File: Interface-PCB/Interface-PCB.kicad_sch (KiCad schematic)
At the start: 17 parts, among them J1 BARREL_JACK_PAD, J2 BARREL_JACK_PAD, J3 GPIO_DEBUG_HEADER, J4 RASPBERRYPI_GPIO_CONN_HEADER, M1 PERISTALTIC_PUMP, M2 PERISTALTIC_PUMP, M3 PERISTALTIC_PUMP, U1 TB6612FNG_BREAKOUT, U2 TB6612FNG_BREAKOUT

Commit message: Add silkscreen and logos to PCB
Complete silkscreen layer on PCB
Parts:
- added G1: PLANTER_LOGO_8mm, Interface-PCB:PLANTER_LOGO_30MM_SILKSCREEN, symbol Interface-PCB:PLANTER_LOGO_8mm
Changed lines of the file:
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@@
   (symbol (lib_id "Interface-PCB:PLANTER_LOGO_8mm") (at 247.65 29.21 0) (unit 1)
     (in_bom yes) (on_board yes) (fields_autoplaced)
-    (property "Reference" "#G1" (id 0) (at 247.65 17.3277 0)
+    (property "Reference" "G1" (id 0) (at 247.65 17.3277 0)
       (effects (font (size 1.27 1.27)) hide)
     )
@@
       (effects (font (size 1.27 1.27)) hide)
     )
-    (property "Footprint" "" (id 2) (at 247.65 29.21 0)
+    (property "Footprint" "Interface-PCB:PLANTER_LOGO_30MM_SILKSCREEN" (id 2) (at 247.65 29.21 0)
       (effects (font (size 1.27 1.27)) hide)
     )
@@
       (reference "#FLG04") (unit 1) (value "PWR_FLAG") (footprint "")
     )
-    (path "/6ae23f34-90ad-41bf-a46e-855f1c65bb29"
-      (reference "#G1") (unit 1) (value "PLANTER_LOGO_8mm") (footprint "")
-    )
     (path "/00000000-0000-0000-0000-000063fcc8a0"
       (reference "#GND01") (unit 1) (value "GND") (footprint "XXX-00000")
@@
       (reference "D3") (unit 1) (value "5V_ON") (footprint "AA_Custom_Components:LED_SS_1206_3216Metric_Pad1.42x1.75mm_HandSolder")
     )
+    (path "/6ae23f34-90ad-41bf-a46e-855f1c65bb29"
+      (reference "G1") (unit 1) (value "PLANTER_LOGO_8mm") (footprint "Interface-PCB:PLANTER_LOGO_30MM_SILKSCREEN")
+    )
     (path "/00000000-0000-0000-0000-000063bd3cac"
       (reference "H1") (unit 1) (value "MountingHole") (footprint "MountingHole:MountingHole_3.2mm_M3_Pad")
@@
       (reference "M3") (unit 1) (value "PERISTALTIC_PUMP") (footprint "AA_Custom_Components:PowerPad_Pair_5.0x5.0mm")
     )
+    (path "/00000000-0000-0000-0000-00006375997b/179f68f0-a496-4478-807a-8a228ac1fdea"
+      (reference "N1") (unit 1) (value "CENTER_POS") (footprint "AA_Custom_Components:Polarity_Center_Positive_7.5mm_SilkScreen")
+    )
+    (path "/00000000-0000-0000-0000-00006375997b/2c5f3129-e0cd-43fe-afad-b677bf741a53"
+      (reference "N2") (unit 1) (value "CENTER_POS") (footprint "AA_Custom_Components:Polarity_Center_Positive_7.5mm_SilkScreen")
+    )
+    (path "/00000000-0000-0000-0000-00006375997b/7412de6c-86c2-4352-a654-eb3ac80aac75"
+      (reference "N3") (unit 1) (value "KiCad") (footprint "Symbol:KiCad-Logo2_8mm_SilkScreen")
+    )
     (path "/00000000-0000-0000-0000-00006375997b/00000000-0000-0000-0000-000063bd2f18"

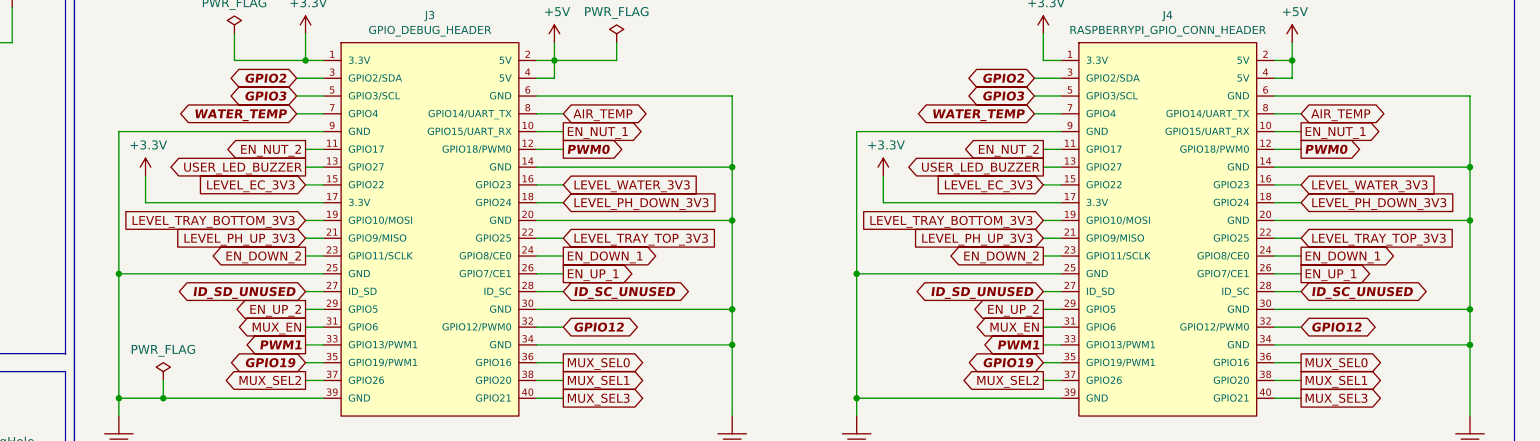
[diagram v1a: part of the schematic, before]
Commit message: Swap more pin assignments
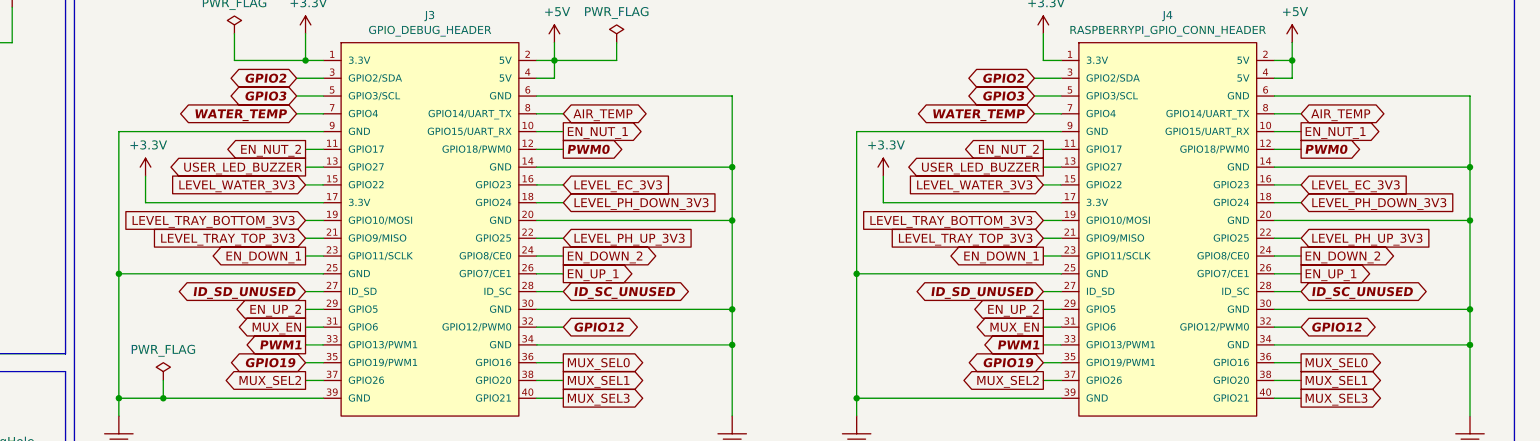
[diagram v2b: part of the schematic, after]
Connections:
- net EN_DOWN_1: now also J3.23 (GPIO11/SCLK), J4.23 (GPIO11/SCLK); no longer J3.24 (GPIO8/CE0), J4.24 (GPIO8/CE0)
- net EN_DOWN_2: now also J3.24 (GPIO8/CE0), J4.24 (GPIO8/CE0); no longer J3.23 (GPIO11/SCLK), J4.23 (GPIO11/SCLK)
- net LEVEL_EC_3V3: now also J3.16 (GPIO23), J4.16 (GPIO23); no longer J3.15 (GPIO22), J4.15 (GPIO22)
- net LEVEL_PH_UP_3V3: now also J3.22 (GPIO25), J4.22 (GPIO25); no longer J3.21 (GPIO9/MISO), J4.21 (GPIO9/MISO)
- net LEVEL_TRAY_TOP_3V3: now also J3.21 (GPIO9/MISO), J4.21 (GPIO9/MISO); no longer J3.22 (GPIO25), J4.22 (GPIO25)
- net LEVEL_WATER_3V3: now also J3.15 (GPIO22), J4.15 (GPIO22); no longer J3.16 (GPIO23), J4.16 (GPIO23)

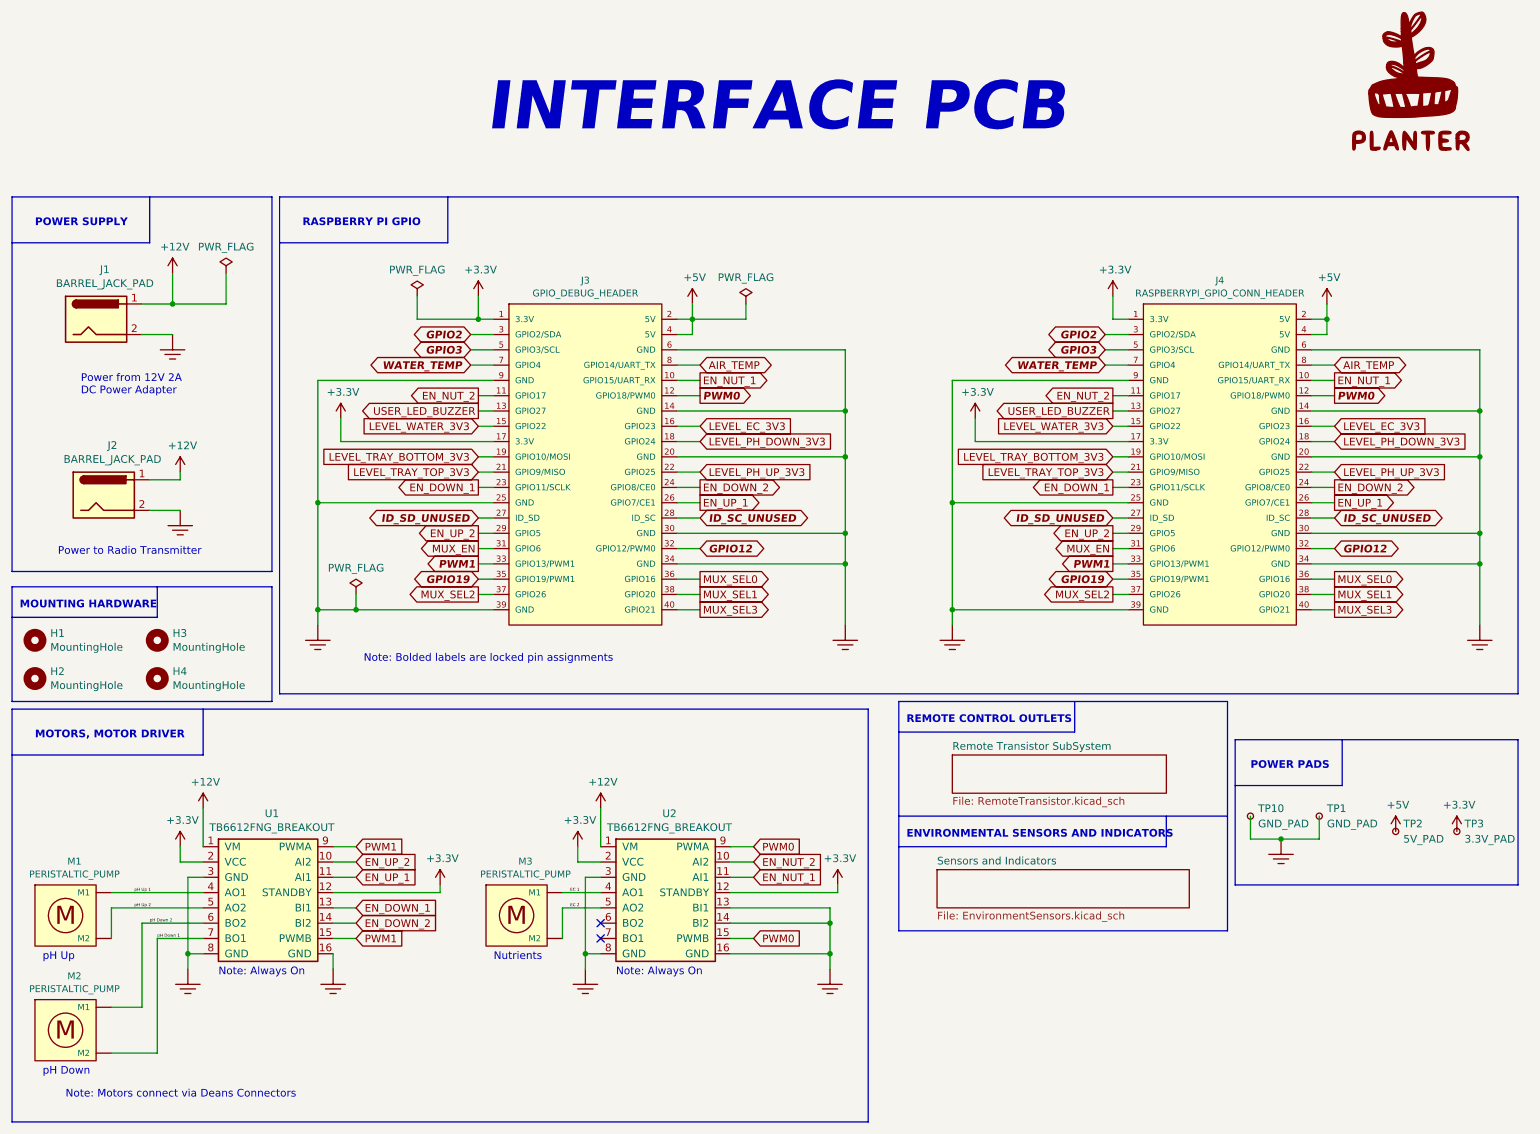
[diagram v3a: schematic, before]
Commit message: Add 3.3V LDO Regulator and Barrel Jack Connectors
- Add mounted barrel jack connectors for 12V and 5V
- Add 5V to 3.3V LDO breakout board
- Adjust silkscreen
- Export and verify Gerbers
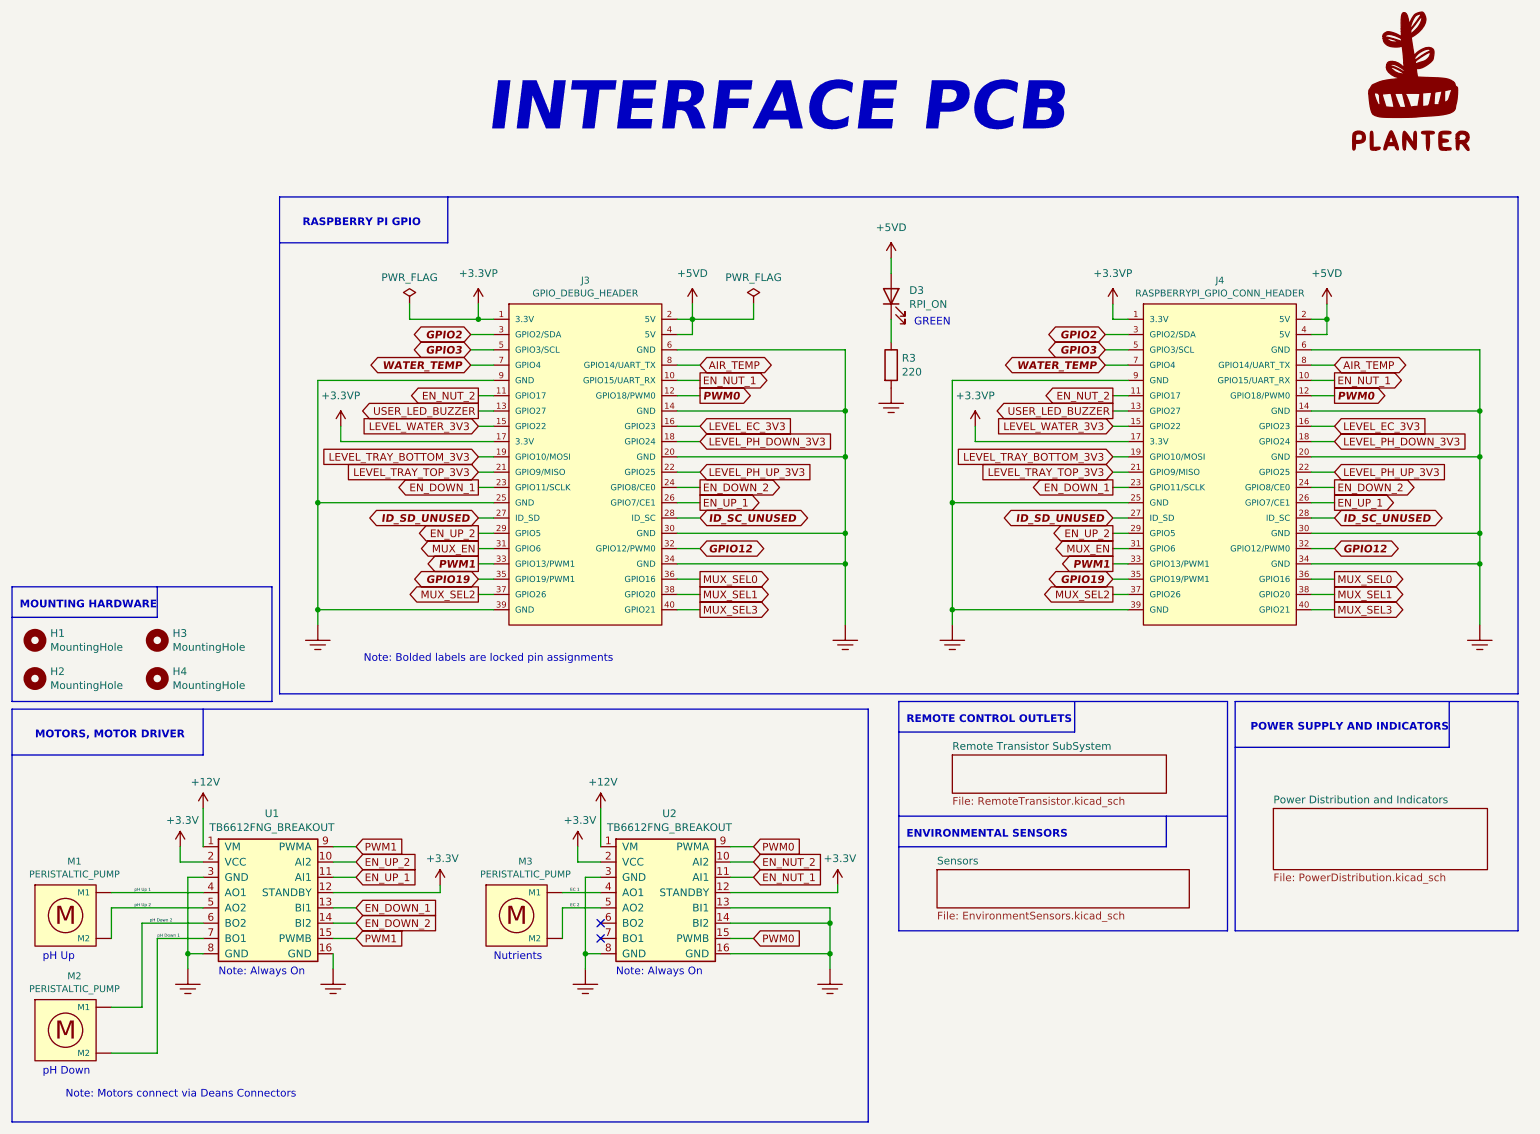
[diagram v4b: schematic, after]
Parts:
- removed J1, J2: BARREL_JACK_PAD, AA_Custom_Components:PowerPad_Pair_5.0x5.0mm, symbol AA_Custom_Components:BARREL_JACK_PAD
- removed TP1, TP10: GND_PAD, AA_Custom_Components:TestPoint_Pad_5.0x5.0mm, symbol Connector:TestPoint_Small
- removed TP2: 5V_PAD, AA_Custom_Components:TestPoint_Pad_5.0x5.0mm, symbol Connector:TestPoint_Small
- removed TP3: 3.3V_PAD, AA_Custom_Components:TestPoint_Pad_5.0x5.0mm, symbol Connector:TestPoint_Small
- added D3: RPI_ON, AA_Custom_Components:LED_SS_1206_3216Metric_Pad1.42x1.75mm_HandSolder, symbol Device:LED
- added R3: 220, AA_Custom_Components:R_SS_Axial_DIN0207_L6.3mm_D2.5mm_P10.16mm_Horizontal, symbol Device:R
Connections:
- net +3V3: no longer J3.1 (3.3V), J3.17 (3.3V), J4.1 (3.3V), J4.17 (3.3V)
- net GND: now also R3.2
- net +5V renamed +5VD
- net +5VD: now also D3.2 (A)
- new net: D3.1 (K), R3.1
- new net +3.3VP: J3.1 (3.3V), J3.17 (3.3V), J4.1 (3.3V), J4.17 (3.3V)
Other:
- sheet Sensors and Indicators renamed Sensors
- added sheet Power Distribution and Indicators (PowerDistribution.kicad_sch)
- note added: "ENVIRONMENTAL SENSORS"
- note added: "GREEN"
- note added: "POWER SUPPLY AND INDICATORS"
- note removed: "ENVIRONMENTAL SENSORS AND INDICATORS"
- note removed: "POWER PADS"
- note removed: "POWER SUPPLY"
- note removed: "Power from 12V 2A DC Power Adapter"
- note removed: "Power to Radio Transmitter"
